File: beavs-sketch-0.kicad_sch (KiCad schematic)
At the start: 31 parts, among them J1 USB_C_Receptacle_USB2.0_16P, J3 Conn_01x02, J5 Conn_01x02, Q1 SiS402DN, Q2 SiS402DN, U15 SN74LVC8T245, U16 SRV05-4, U17 SRV05-4, U19 LM74502, U7 AMS1117-3.3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

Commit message: I may be stupid
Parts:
- removed C46: 220n, Capacitor_SMD:C_0402_1005Metric, symbol Device:C_Small
- removed R2: 100, Resistor_SMD:R_0402_1005Metric, symbol Device:R_Small
- removed U19: LM74502, Package_TO_SOT_SMD:SOT-23-8, symbol beavs-symbols:LM74502
- added Q3: AO3401A, Package_TO_SOT_SMD:SOT-23, symbol Transistor_FET:AO3401A
- added R14: R_Small, Resistor_SMD:R_0402_1005Metric, symbol Device:R_Small
- added R2: R, Resistor_SMD:R_0805_2012Metric, symbol Device:R
- added U19: LM74700, Package_TO_SOT_SMD:SOT-23-6, symbol Power_Management:LM74700
- C45: value 220n -> C_Small; LCSC C16772 -> (none)
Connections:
- net +BATT: now also U19.4 (CATHODE)
- net GND: now also U19.2 (GND)
- net at J3.2 (Pin_2), Q1.5 (D): now also R2.1
- net at Q1.4 (G): now also Q3.3 (D), R14.2; no longer Q2.4 (G)
- net at C45.1: now also Q1.1 (S), Q1.2 (S), Q1.3 (S), Q2.1 (S), Q2.2 (S), Q2.3 (S), R14.1, R2.2, U19.6 (ANODE)
- net at C45.2: now also U19.1 (VCAP)
- new net: Q2.4 (G), Q3.2 (S), U19.5 (GATE)
- new net mcu/SERVO_POWER_EN: Q3.1 (G)
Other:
- sheet mcu ports: added SERVO_POWER_EN; removed none
- moved on the sheet: C15, C16, C17, C18, D1, D2, D3, D4, D5, D6, D7, D8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

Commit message: definitely stupid
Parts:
- removed Q1: SiS402DN, Package_SO:Vishay_PowerPAK_1212-8_Single, symbol Transistor_FET:Q_NMOS_SSSGD_AvalancheRated
- removed Q3: AO3401A, Package_TO_SOT_SMD:SOT-23, symbol Transistor_FET:AO3401A
- removed R14: R_Small, Resistor_SMD:R_0402_1005Metric, symbol Device:R_Small
- added C46: 220n, Capacitor_SMD:C_0402_1005Metric, symbol Device:C_Small
- added D11: D_Schottky, Diode_SMD:D_SOD-123, symbol Device:D_Schottky
- C45: value C_Small -> 220n; LCSC (none) -> C16772
- R2: value R -> 300; footprint Resistor_SMD:R_0805_2012Metric -> Resistor_SMD:R_1206_3216Metric
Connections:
- net +BATT: now also D11.1 (K)
- net GND: now also C46.2
- net mcu/SERVO_POWER_EN: now also U19.3 (EN)
- net at C45.1, Q2.1 (S), Q2.2 (S)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: now also J3.2 (Pin_2), R2.1, C46.1; no longer R2.2
- new net: D11.2 (A), R2.2
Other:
- moved on the sheet: J3, R2, U19

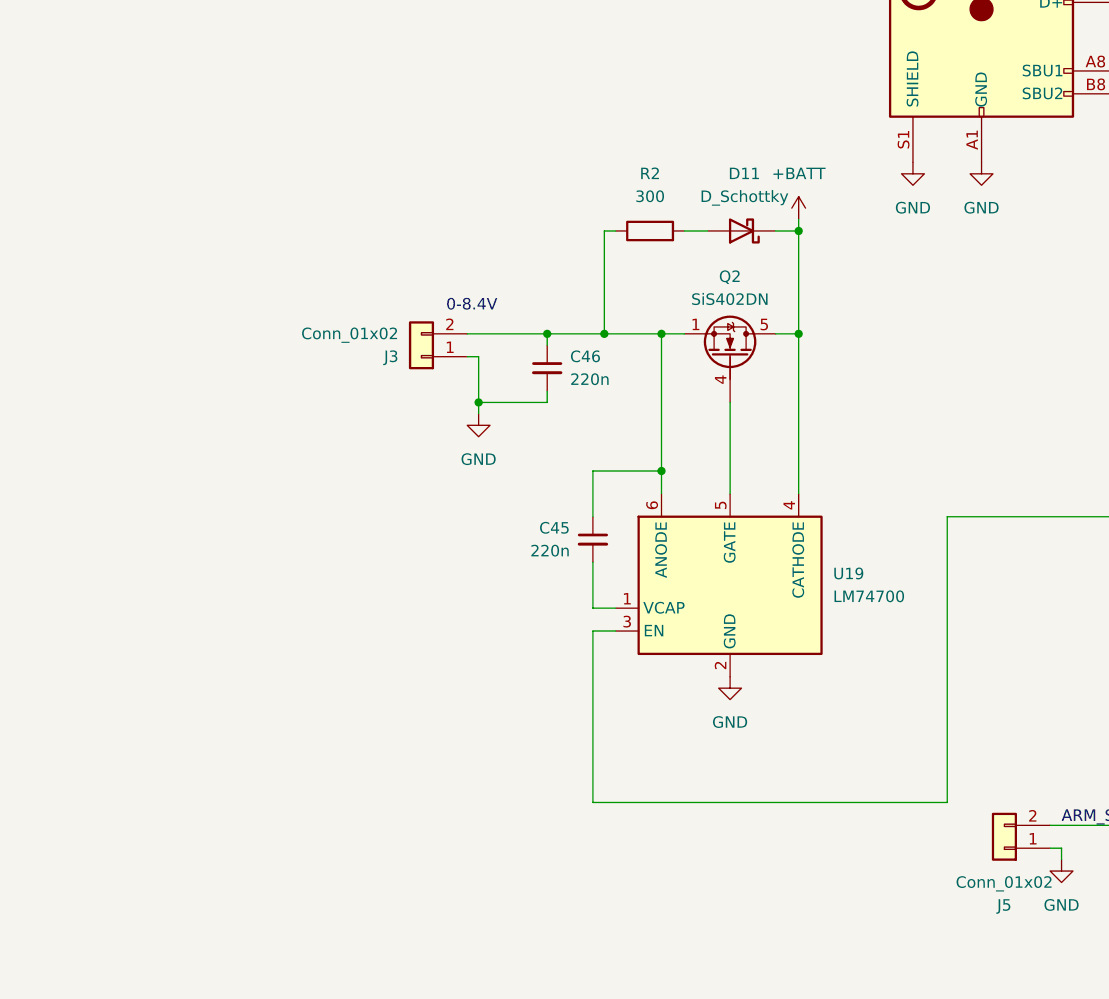
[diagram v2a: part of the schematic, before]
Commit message: swapped to a reverse polarity + inrush scheme that might actually work
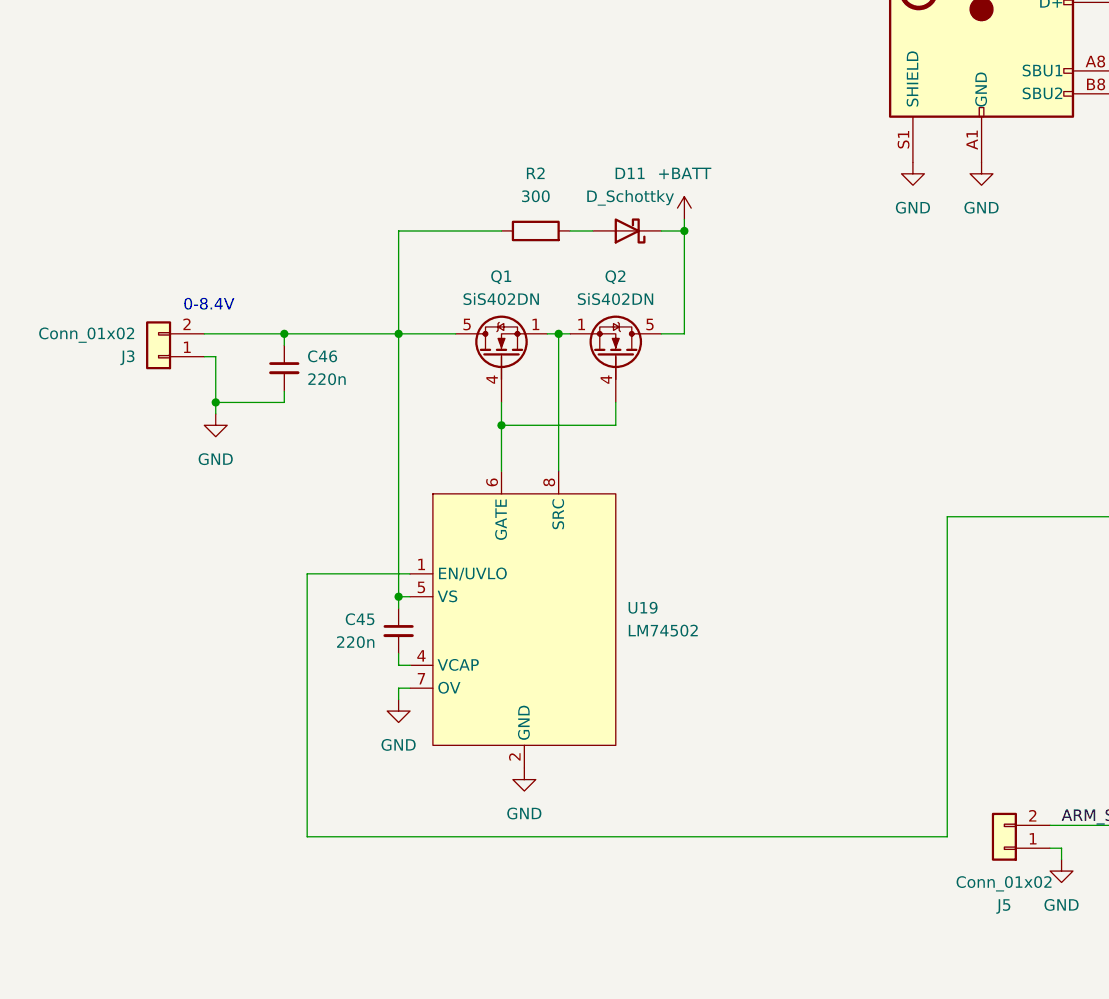
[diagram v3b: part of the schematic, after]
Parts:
- removed U19: LM74700, Package_TO_SOT_SMD:SOT-23-6, symbol Power_Management:LM74700
- added Q1: SiS402DN, Package_SO:Vishay_PowerPAK_1212-8_Single, symbol Transistor_FET:Q_NMOS_SSSGD_AvalancheRated
- added U19: LM74502, Package_TO_SOT_SMD:SOT-23-8, symbol beavs-symbols:LM74502
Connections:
- net GND: now also U19.2 (GND), U19.7 (OV)
- net mcu/SERVO_POWER_EN: now also U19.1 (EN/UVLO)
- net at C45.1, C46.1, J3.2 (Pin_2)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: now also Q1.5 (D), U19.5 (VS); no longer Q2.1 (S), Q2.2 (S), Q2.3 (S)
- net at C45.2: now also U19.4 (VCAP)
- net at Q2.4 (G): now also Q1.4 (G), U19.6 (GATE)
- new net: Q1.1 (S), Q1.2 (S), Q1.3 (S), Q2.1 (S), Q2.2 (S), Q2.3 (S), U19.8 (SRC)
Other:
- moved on the sheet: C46, D11, J3, Q2, R2

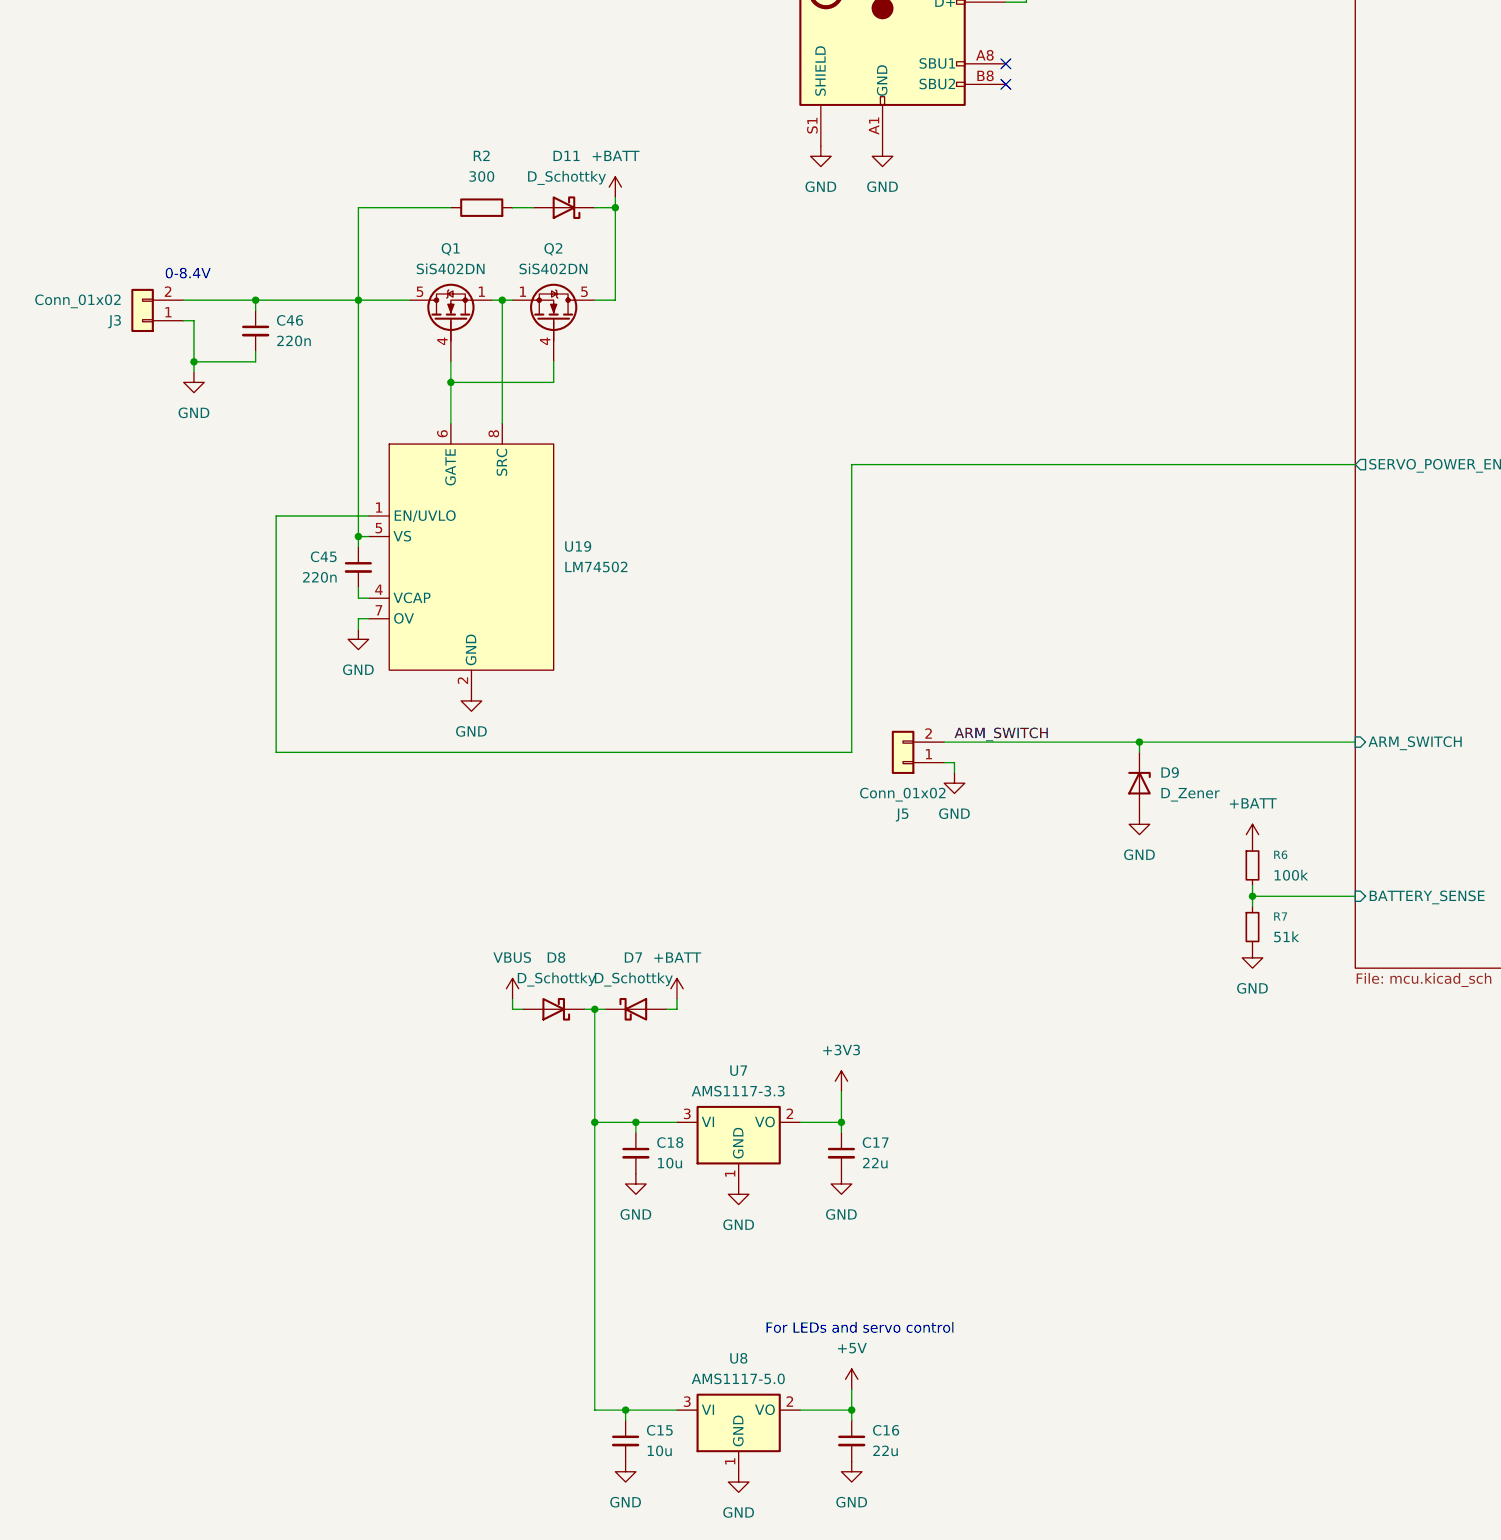
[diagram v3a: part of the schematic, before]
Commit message: finished power, checked most sensor schematics
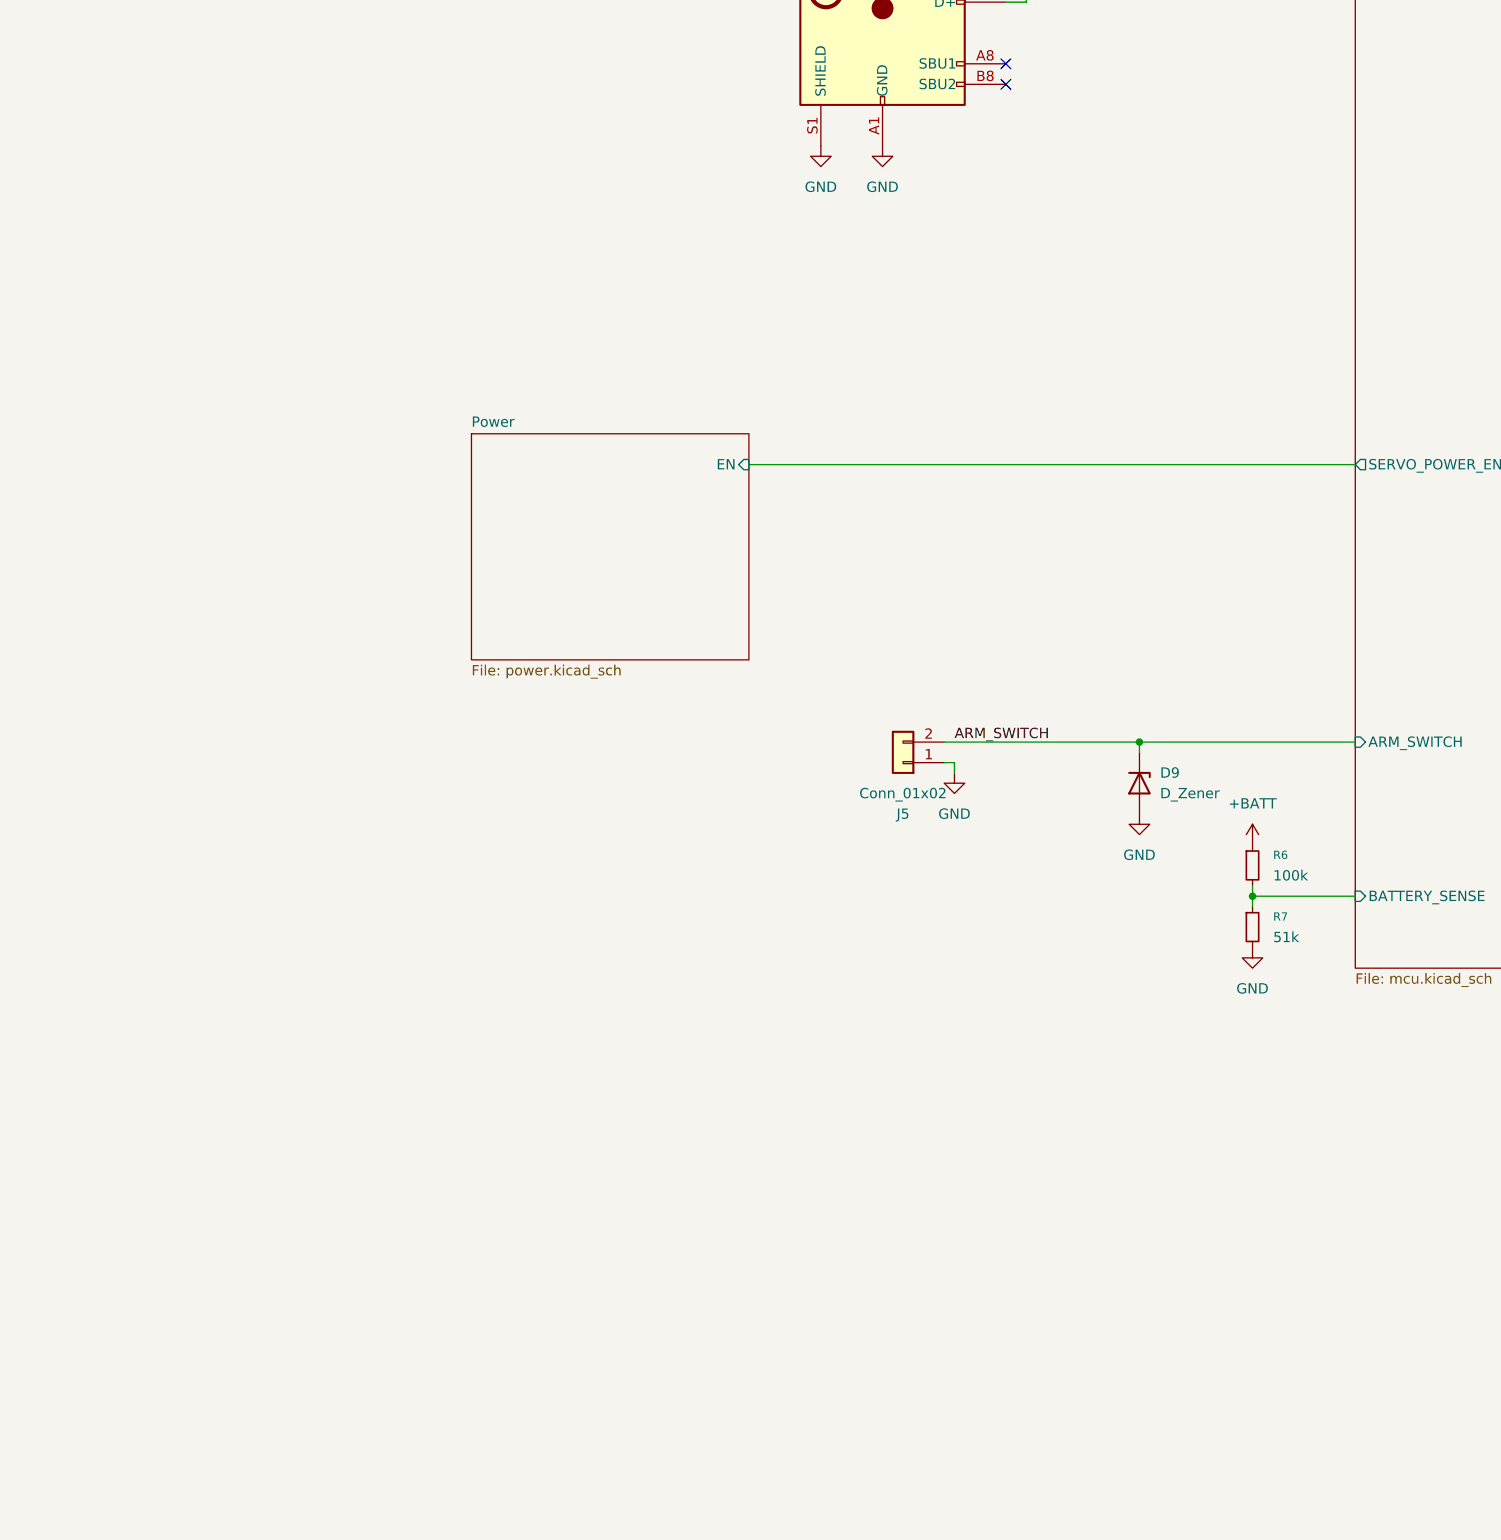
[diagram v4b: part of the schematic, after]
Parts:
- removed C15, C18: 10u, Capacitor_SMD:C_0603_1608Metric, symbol Device:C_Small
- removed C16, C17: 22u, Capacitor_SMD:C_0603_1608Metric, symbol Device:C_Small
- removed C45, C46: 220n, Capacitor_SMD:C_0402_1005Metric, symbol Device:C_Small
- removed D11, D7, D8: D_Schottky, Diode_SMD:D_SOD-123, symbol Device:D_Schottky
- removed J3: Conn_01x02, Connector_AMASS:AMASS_XT30UPB-M_1x02_P5.0mm_Vertical, symbol Connector_Generic:Conn_01x02
- removed Q1, Q2: SiS402DN, Package_SO:Vishay_PowerPAK_1212-8_Single, symbol Transistor_FET:Q_NMOS_SSSGD_AvalancheRated
- removed R2: 300, Resistor_SMD:R_1206_3216Metric, symbol Device:R
- removed U19: LM74502, Package_TO_SOT_SMD:SOT-23-8, symbol beavs-symbols:LM74502
- removed U7: AMS1117-3.3, Package_TO_SOT_SMD:SOT-223-3_TabPin2, symbol Regulator_Linear:AMS1117-3.3
- removed U8: AMS1117-5.0, Package_TO_SOT_SMD:SOT-223-3_TabPin2, symbol Regulator_Linear:AMS1117-5.0
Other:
- added sheet Power (power.kicad_sch)
- note removed: "0-8.4V"
- note removed: "For LEDs and servo control"

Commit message: bigger pours for FETs, various cleanup, switching to different level shifter
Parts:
- J5: digikey (none) -> 455-1704-ND
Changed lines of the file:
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@@
+			)
+		)
+		(property "digikey" "455-1704-ND"
+			(at 115.57 172.72 0)
+			(effects
+				(font
+					(size 1.27 1.27)
+				)
+				(hide yes)
 			)
 		)
@@
 			)
 		)
+		(property "digikey" ""
+			(at 349.25 167.64 0)
+			(effects
+				(font
+					(size 1.27 1.27)
+				)
+				(hide yes)
+			)
+		)
 		(pin "1"
 		)
@@
 			)
 		)
+		(property "digikey" ""
+			(at 144.78 175.26 90)
+			(effects
+				(font
+					(size 1.27 1.27)
+				)
+				(hide yes)
+			)
+		)
 		(pin "1"
 		)
@@
 			)
 		)
+		(property "digikey" ""
+			(at 337.82 60.96 0)
+			(effects
+				(font
+					(size 1.27 1.27)
+				)
+				(hide yes)
+			)
+		)
 		(pin "5"
 		)
@@
 			)
 		)
+		(property "digikey" ""
+			(at 365.76 167.64 0)
+			(effects
+				(font
+					(size 1.27 1.27)
+				)
+				(hide yes)
+			)
+		)
 		(pin "1"
 		)
@@
 			)
 		)
+		(property "digikey" ""
+			(at 113.03 73.66 0)
+			(effects
+				(font
+					(size 1.27 1.27)
+				)
+				(hide yes)
+			)
+		)
 		(pin "A1"
 		)
@@
 			)
 		)
+		(property "digikey" ""
+			(at 316.23 167.64 0)
+			(effects
+				(font
+					(size 1.27 1.27)
+				)
+				(hide yes)
+			)
+		)
 		(pin "1"
 		)
@@
 			)
 		)
+		(property "digikey" ""
+			(at 133.35 63.5 90)
+			(effects
+				(font
+					(size 1.27 1.27)
+				)
+				(hide yes)
+			)
+		)
 		(pin "2"
 		)
@@
 			)
 		)
+		(property "digikey" ""
+			(at 293.37 60.96 0)
+			(effects
+				(font
+					(size 1.27 1.27)
+				)
+				(hide yes)
+			)
+		)
 		(pin "5"
 		)
@@
 			)
 		)
+		(property "digikey" ""
+			(at 158.75 193.04 0)
+			(effects
+				(font
+					(size 1.27 1.27)
+				)
+				(hide yes)
+			)
+		)
 		(pin "2"
 		)
@@
 			)
 		)
+		(property "digikey" ""
+			(at 382.27 167.64 0)
+			(effects
+				(font
+					(size 1.27 1.27)
+				)
+				(hide yes)
+			)
+		)
 		(pin "1"
 		)
@@
 			)
 		)
+		(property "digikey" ""
+			(at 243.84 129.54 0)
+			(effects
+				(font
+					(size 1.27 1.27)
+				)
+				(hide yes)
+			)
+		)
 		(pin "2"
 		)
@@
 			)
 		)
+		(property "digikey" ""
+			(at 158.75 185.42 0)
+			(effects
+				(font
+					(size 1.27 1.27)
+				)
+				(hide yes)
+			)
+		)
 		(pin "2"
 		)
@@
 		)
 		(property "LCSC" "C2909058"
+			(at 299.72 167.64 0)
+			(effects
+				(font
+					(size 1.27 1.27)
+				)
+				(hide yes)
+			)
+		)
+		(property "digikey" ""
 			(at 299.72 167.64 0)
 			(effects
@@
 			)
 		)
+		(property "digikey" ""
+			(at 133.35 66.04 90)
+			(effects
+				(font
+					(size 1.27 1.27)
+				)
+				(hide yes)
+			)
+		)
 		(pin "2"
 		)
@@
 			(at 332.74 167.64 0)
 			(effects
+				(font
+					(size 1.27 1.27)
+				)
+				(hide yes)
+			)
+		)
+		(property "digikey" ""
+			(at 332.74 167.64 0)
+			(effects

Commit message: changes apparently but idk what
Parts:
- removed U15: SN74LVC8T245, Package_SO:TSSOP-24_4.4x7.8mm_P0.65mm, symbol Logic_LevelTranslator:SN74LVC8T245
- added U15: SN74LVC4245APW, Package_SO:TSSOP-24_4.4x7.8mm_P0.65mm, symbol beavs-symbols:SN74LVC4245A
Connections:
- net +3V3: now also U15.23 (V_{CCB}), U15.24 (V_{CCB})
- net +5V: now also U15.1 (V_{CCA})
- net GND: now also U15.11 (GND), U15.12 (GND), U15.13 (GND), U15.14 (B8), U15.22 (~{OE})
- net mcu/LEVELSHIFT_DIR: now also U15.2 (DIR)
- net mcu/M_LED_D: now also U15.21 (B1)
- net mcu/M_S1: now also U15.15 (B7)
- net mcu/M_S2: now also U15.16 (B6)
- net mcu/M_S3: now also U15.17 (B5)
- net mcu/M_S4: now also U15.18 (B4)
- net mcu/M_S5: now also U15.19 (B3)
- net mcu/M_S6: now also U15.20 (B2)
- net servos/S1: now also U15.9 (A7)
- net servos/S2: now also U15.8 (A6)
- net servos/S3: now also U15.7 (A5)
- net servos/S4: now also U15.6 (A4)
- net servos/S5: now also U15.5 (A3)
- net servos/S6: now also U15.4 (A2)
- net at D1.4 (DIN): now also U15.3 (A1)
